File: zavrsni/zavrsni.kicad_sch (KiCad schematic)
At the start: 81 parts, among them J1 Barrel_Jack_MountingPin, J2 SameSky 6.35 horizontal jack, J3 USB_B, J4 SameSky 6.35 horizontal jack, SW1 EC11, U1 TL072, U10 TL072, U2 LM317_TO-220, U3 LM317_TO-220, U4 TL074, U6 WeAct STM32F411CEU6 v3.0, U7 TL074, U8 CS4271, U9 TL072

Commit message: KiCad 10
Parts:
- removed C1: 100n, Capacitor_THT:C_Disc_D5.0mm_W2.5mm_P5.00mm, symbol Device:C_Small
- removed R21: 10k, Resistor_THT:R_Axial_DIN0207_L6.3mm_D2.5mm_P2.54mm_Vertical, symbol Device:R
- removed U1, U10, U9: TL072, Package_DIP:DIP-8_W7.62mm, symbol Amplifier_Operational:TL072
- added C1: 47u, Capacitor_THT:CP_Radial_D5.0mm_P2.50mm, symbol Device:C_Polarized_Small
- added C26, C27: 10u, Capacitor_THT:CP_Radial_D5.0mm_P2.50mm, symbol Device:C_Polarized_Small
- added U1: TL074, Package_DIP:DIP-14_W7.62mm, symbol Amplifier_Operational:TL074
- added unit 5 of U4
- added unit 2 of U4
- added U9: LM358, Package_DIP:DIP-8_W7.62mm, symbol Amplifier_Operational:LM358
- C3: value 680u -> 10u; footprint Capacitor_THT:CP_Radial_D8.0mm_P2.50mm -> Capacitor_THT:CP_Radial_D5.0mm_P2.50mm
- R1, R2: value 51k -> 10k
- SW_BNK+1, SW_BNK-1, SW_PRE+1, SW_PRE-1, SW_VOL+1, SW_VOL-1: footprint Button_Switch_THT:SW_PUSH_6mm_H7.3mm -> Button_Switch_THT:SW_PUSH_6mm_H13mm
- U5: value ~ -> (none)
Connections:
- net GNDPWR: now also J1.3 (MountPin), C1.2, C26.2, C27.2; no longer J1.MP (MountPin)
- net GNDREF: now also C1.1, U9.1, U9.2 (-); no longer C3.1
- net IN: now also U1.5 (+)
- net VREF_ADC: now also U4.8, U4.9 (-)
- net at C8.1, R7.1, R8.1: now also U1.9 (-); no longer U4.2 (-)
- net at C8.2, R11.2, R8.2: now also U1.8; no longer U4.1
- net at R6.1: now also U1.6 (-), U1.7
- net at R4.2, R5.1, U2.1 (ADJ): now also C26.1
- net at C25.1: now also U7.1, U7.2 (-)
- net at C24.1, R28.2: now also U7.3 (+)
- net at C18.1, C20.1, U8.15 (VQ1): now also U4.10 (+)
- net at C6.1, R6.2: now also U1.10 (+); no longer U4.3 (+)
- net at R12.2, R13.1: now also U1.12 (+); no longer U4.10 (+)
- net at R24.2, R26.2: now also U4.12 (+)
- net at D1.2 (A), D2.1 (K), R11.1: now also U4.2 (-), U1.13 (-), U4.5 (+); no longer U4.13 (-), U4.9 (-), U7.3 (+)
- net at C23.1, R25.1, R27.2: now also U4.13 (-)
- net at R10.1, R9.2, U3.1 (ADJ): now also C27.1
- net at R1.1, R2.2: now also C3.1, U9.3 (+), U9.5 (+)
- net at R14.2, R15.1: now also U4.3 (+); no longer U4.12 (+)
- net at C23.2, R27.1, R28.1: now also U4.14
- net at D1.1 (K): now also U1.14; no longer U4.8
- net at D2.2 (A): now also U4.1; no longer U4.14
- new net: U9.6 (-), U9.7
- new net: C12.1, U4.6 (-), U4.7
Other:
- note added: "Napajanje"
- note removed: "Ulazni razdvojnik (buffer)"
- moved on the sheet: C10, C11, C12, C13, C14, C15, C16, C17, C18, C19, C2, C20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

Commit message: Started work on the PCB. Started drawing the codec/STM32 part of the layout.
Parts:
- removed U4, U7: TL074, Package_DIP:DIP-14_W7.62mm, symbol Amplifier_Operational:TL074
- added C28: 10u, Capacitor_THT:CP_Radial_D5.0mm_P2.50mm, symbol Device:C_Polarized_Small
- added C29, C30, C31, C33: 100n, Capacitor_THT:C_Disc_D5.0mm_W2.5mm_P5.00mm, symbol Device:C_Small
- added C32: 100u, Capacitor_THT:CP_Radial_D5.0mm_P2.50mm, symbol Device:C_Polarized_Small
- added D3, D4, D5, D6, D7, D8: LED, LED_THT:LED_D3.0mm, symbol Device:LED
- added JP_LIM1: SolderJumper_2_Open, Jumper:SolderJumper-2_P1.3mm_Open_RoundedPad1.0x1.5mm, symbol Jumper:SolderJumper_2_Open
- added R21: 100, Resistor_THT:R_Axial_DIN0207_L6.3mm_D2.5mm_P5.08mm_Vertical, symbol Device:R
- added R30, R31, R32, R33, R34, R35: 1k, Resistor_THT:R_Axial_DIN0207_L6.3mm_D2.5mm_P2.54mm_Vertical, symbol Device:R
- added TP_3V3, TP_5V1, TP_FILT1, TP_LIM1: Conn_01x01, Connector_PinHeader_2.54mm:PinHeader_1x01_P2.54mm_Vertical, symbol Connector_Generic:Conn_01x01
- added TP_CODEC1: Conn_01x05, Connector_PinHeader_2.54mm:PinHeader_1x05_P2.54mm_Vertical, symbol Connector_Generic:Conn_01x05
- added TP_OUT1: Conn_01x02, Connector_PinHeader_2.54mm:PinHeader_1x02_P2.54mm_Vertical, symbol Connector_Generic:Conn_01x02
- added unit 1 of U1
- added U10, U7: TL072, Package_DIP:DIP-8_W7.62mm, symbol Amplifier_Operational:TL072
- R16, R19: footprint Resistor_THT:R_Axial_DIN0207_L6.3mm_D2.5mm_P5.08mm_Vertical -> Resistor_THT:R_Axial_DIN0207_L6.3mm_D2.5mm_P10.16mm_Horizontal
- R17: footprint Resistor_THT:R_Axial_DIN0207_L6.3mm_D2.5mm_P5.08mm_Vertical -> Resistor_THT:R_Axial_DIN0207_L6.3mm_D2.5mm_P15.24mm_Horizontal
- R22: footprint Resistor_THT:R_Axial_DIN0207_L6.3mm_D2.5mm_P5.08mm_Vertical -> Resistor_THT:R_Axial_DIN0207_L6.3mm_D2.5mm_P2.54mm_Vertical
- R23: footprint Resistor_THT:R_Axial_DIN0207_L6.3mm_D2.5mm_P2.54mm_Vertical -> Resistor_THT:R_Axial_DIN0207_L6.3mm_D2.5mm_P5.08mm_Vertical
- U6: footprint Package_DIP:DIP-40_W15.24mm_Socket -> ljepi:STM32F411CEU6 WeAct V3.0
- renumbered J2 to JIN1, J4 to JOUT1
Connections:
- net +3V3: now also TP_3V3.1 (Pin_1)
- net +5V: now also TP_5V1.1 (Pin_1)
- net GNDPWR: now also J3.SH (Shield), U1.11 (V-), U9.4 (V-), C28.2, C29.2, C30.2, C31.2, C32.2, C33.2, D3.1 (K), D4.1 (K), D5.1 (K), D6.1 (K), D7.1 (K), D8.1 (K), U10.4 (V-), U7.4 (V-); no longer J3.5 (Shield)
- net IN: now also U1.3 (+); no longer U1.5 (+)
- net MCU.LRCK: now also TP_CODEC1.2 (Pin_2)
- net MCU.MCLK: now also TP_CODEC1.1 (Pin_1)
- net MCU.SCLK: now also TP_CODEC1.3 (Pin_3)
- net VCC: now also U1.4 (V+), U9.8 (V+), C29.1, C30.1, C31.1, C32.1, C33.1, R21.2, R30.1, R31.1, R32.1, R33.1, R34.1, R35.1, U10.8 (V+), U7.8 (V+); no longer R1.2, R12.1, R14.1
- net VREF_ADC: now also U7.6 (-), U7.7
- net at R22.1, U8.7 (SDIN): now also TP_CODEC1.5 (Pin_5)
- net at C8.1, R7.1, R8.1: now also U1.6 (-); no longer U1.9 (-)
- net at C8.2, R11.2, R8.2: now also U1.7; no longer U1.8
- net at D2.2 (A): now also U1.14
- net at D1.2 (A), D2.1 (K), R11.1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: now also U1.9 (-), JP_LIM1.1 (A), TP_LIM1.1 (Pin_1)
- net at R14.2, R15.1: now also U1.12 (+)
- net at C18.1, C20.1, U8.15 (VQ1): now also U7.5 (+)
- net at C14.1, C15.1, U8.22 (FILT+): now also TP_FILT1.1 (Pin_1)
- net at C21.1, U8.24 (AOUTA-): now also TP_OUT1.1 (Pin_1)
- net at C22.1, U8.25 (AOUTA+): now also TP_OUT1.2 (Pin_2)
- net at R20.1, U8.6 (SDOUT): now also TP_CODEC1.4 (Pin_4)
- net at C6.1, R6.2: now also U1.5 (+); no longer U1.10 (+)
- net at R12.2, R13.1: now also U1.10 (+); no longer U1.12 (+)
- net at C25.1: now also U10.6 (-), U10.7
- net at C24.1, R28.2: now also U10.5 (+)
- net at R24.2, R26.2: now also U10.3 (+)
- net at C12.1: now also U7.1, U7.2 (-)
- net at C23.1, R25.1, R27.2: now also U10.2 (-)
- net at C23.2, R27.1, R28.1: now also U10.1
- net at D1.1 (K): now also U1.8; no longer U1.14
- new net: D4.2 (A), R31.2
- new net: D6.2 (A), R33.2
- new net: D5.2 (A), R32.2
- new net: R6.1, U1.1, U1.2 (-)
- new net: D8.2 (A), R35.2
- new net: JP_LIM1.2 (B), U7.3 (+)
- new net: D7.2 (A), R34.2
- new net: D3.2 (A), R30.2
- new net VCCA: C28.1, R1.2, R12.1, R14.1, R21.1
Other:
- moved on the sheet: C1, C2, C3, C4, C6, C8, D1, D2, H1, H2, H3, H4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

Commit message: PCB almost done.
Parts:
- removed D3, D4, D5, D6, D7, D8: LED, LED_THT:LED_D3.0mm, symbol Device:LED
- removed R30, R31, R32, R33, R34, R35: 1k, Resistor_THT:R_Axial_DIN0207_L6.3mm_D2.5mm_P2.54mm_Vertical, symbol Device:R
- removed TP_3V3, TP_5V1: Conn_01x01, Connector_PinHeader_2.54mm:PinHeader_1x01_P2.54mm_Vertical, symbol Connector_Generic:Conn_01x01
- removed TP_CODEC1: Conn_01x05, Connector_PinHeader_2.54mm:PinHeader_1x05_P2.54mm_Vertical, symbol Connector_Generic:Conn_01x05
- added J2: Conn_01x05, Connector_PinHeader_2.54mm:PinHeader_1x05_P2.54mm_Vertical, symbol Connector_Generic:Conn_01x05
- added JP_3V3, JP_5V1: SolderJumper_2_Open, Jumper:SolderJumper-2_P1.3mm_Open_RoundedPad1.0x1.5mm, symbol Jumper:SolderJumper_2_Open
- R25: footprint Resistor_THT:R_Axial_DIN0207_L6.3mm_D2.5mm_P2.54mm_Vertical -> Resistor_THT:R_Axial_DIN0207_L6.3mm_D2.5mm_P10.16mm_Horizontal
- R26: footprint Resistor_THT:R_Axial_DIN0207_L6.3mm_D2.5mm_P2.54mm_Vertical -> Resistor_THT:R_Axial_DIN0207_L6.3mm_D2.5mm_P7.62mm_Horizontal
- R3: footprint Resistor_THT:R_Axial_DIN0207_L6.3mm_D2.5mm_P2.54mm_Vertical -> Resistor_THT:R_Axial_DIN0207_L6.3mm_D2.5mm_P5.08mm_Vertical
- R6: footprint Resistor_THT:R_Axial_DIN0207_L6.3mm_D2.5mm_P5.08mm_Vertical -> Resistor_THT:R_Axial_DIN0207_L6.3mm_D2.5mm_P7.62mm_Horizontal
- R8: footprint Resistor_THT:R_Axial_DIN0207_L6.3mm_D2.5mm_P5.08mm_Vertical -> Resistor_THT:R_Axial_DIN0207_L6.3mm_D2.5mm_P2.54mm_Vertical
- U2, U3: footprint Package_TO_SOT_THT:TO-220-3_Horizontal_TabDown -> Package_TO_SOT_THT:TO-220-3_Vertical
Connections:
- net +3V3: now also JP_3V3.2 (B); no longer R9.1, U3.2 (VO), U6.20 (3V3)
- net +5V: now also U3.2 (VO), JP_5V1.2 (B); no longer R4.1, U2.2 (VO), U3.3 (VI)
- net BTN.BNK+: now also U6.17 (B9); no longer U6.13 (B5)
- net BTN.BNK-: now also U6.16 (B8); no longer U6.12 (B4)
- net BTN.PRE+: now also U6.13 (B5); no longer U6.17 (B9)
- net BTN.PRE-: now also U6.12 (B4); no longer U6.16 (B8)
- net GNDPWR: now also SW1.S1; no longer SW1.S2
- net MCU.ADC_OUT: now also J2.3 (Pin_3)
- net MCU.DAC_IN: now also J2.2 (Pin_2)
- net MCU.RST: now also J2.1 (Pin_1)
- net MCU.DAC_IN0: now reaches R22.1, U8.7 (SDIN)
- net MCU.ADC_OUT0: now reaches R20.1, U8.6 (SDOUT)
- net MCU.SCLK0: now reaches R16.2, U6.2 (B13)
- net MCU.SCLK0: now also J2.4 (Pin_4)
- net at U6.24 (C15): now also SW1.S2; no longer SW1.S1
- net MCU.LRCK0: now reaches R17.2, U6.1 (B12)
- net MCU.LRCK0: now also J2.5 (Pin_5)
- new net: JP_3V3.1 (A), R9.1, U3.3 (VI)
- new net: JP_5V1.1 (A), R4.1, U2.2 (VO)
- no-connect marks 16 -> 32
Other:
- moved on the sheet: R10, R16, R17, R20, R4, R5, R9

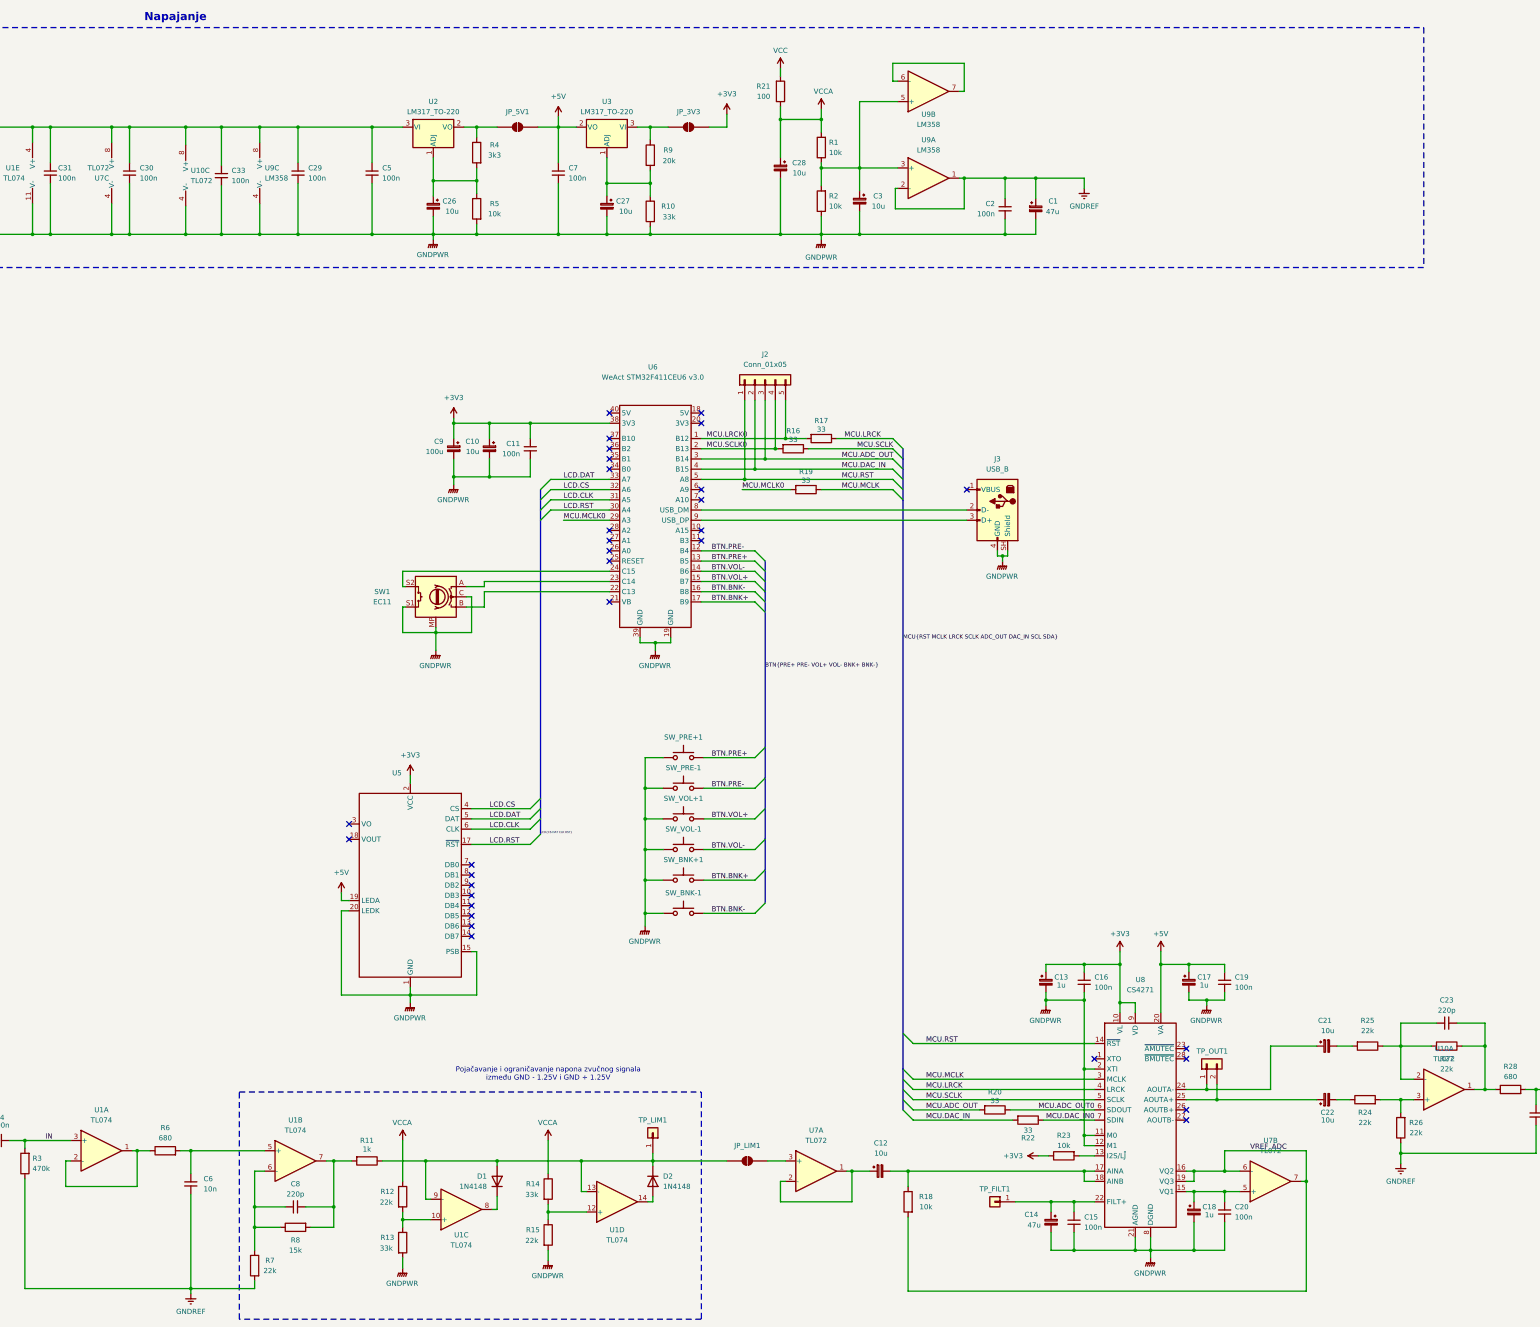
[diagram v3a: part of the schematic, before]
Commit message: PCB done. Code, PCB screw holes and 3D design left
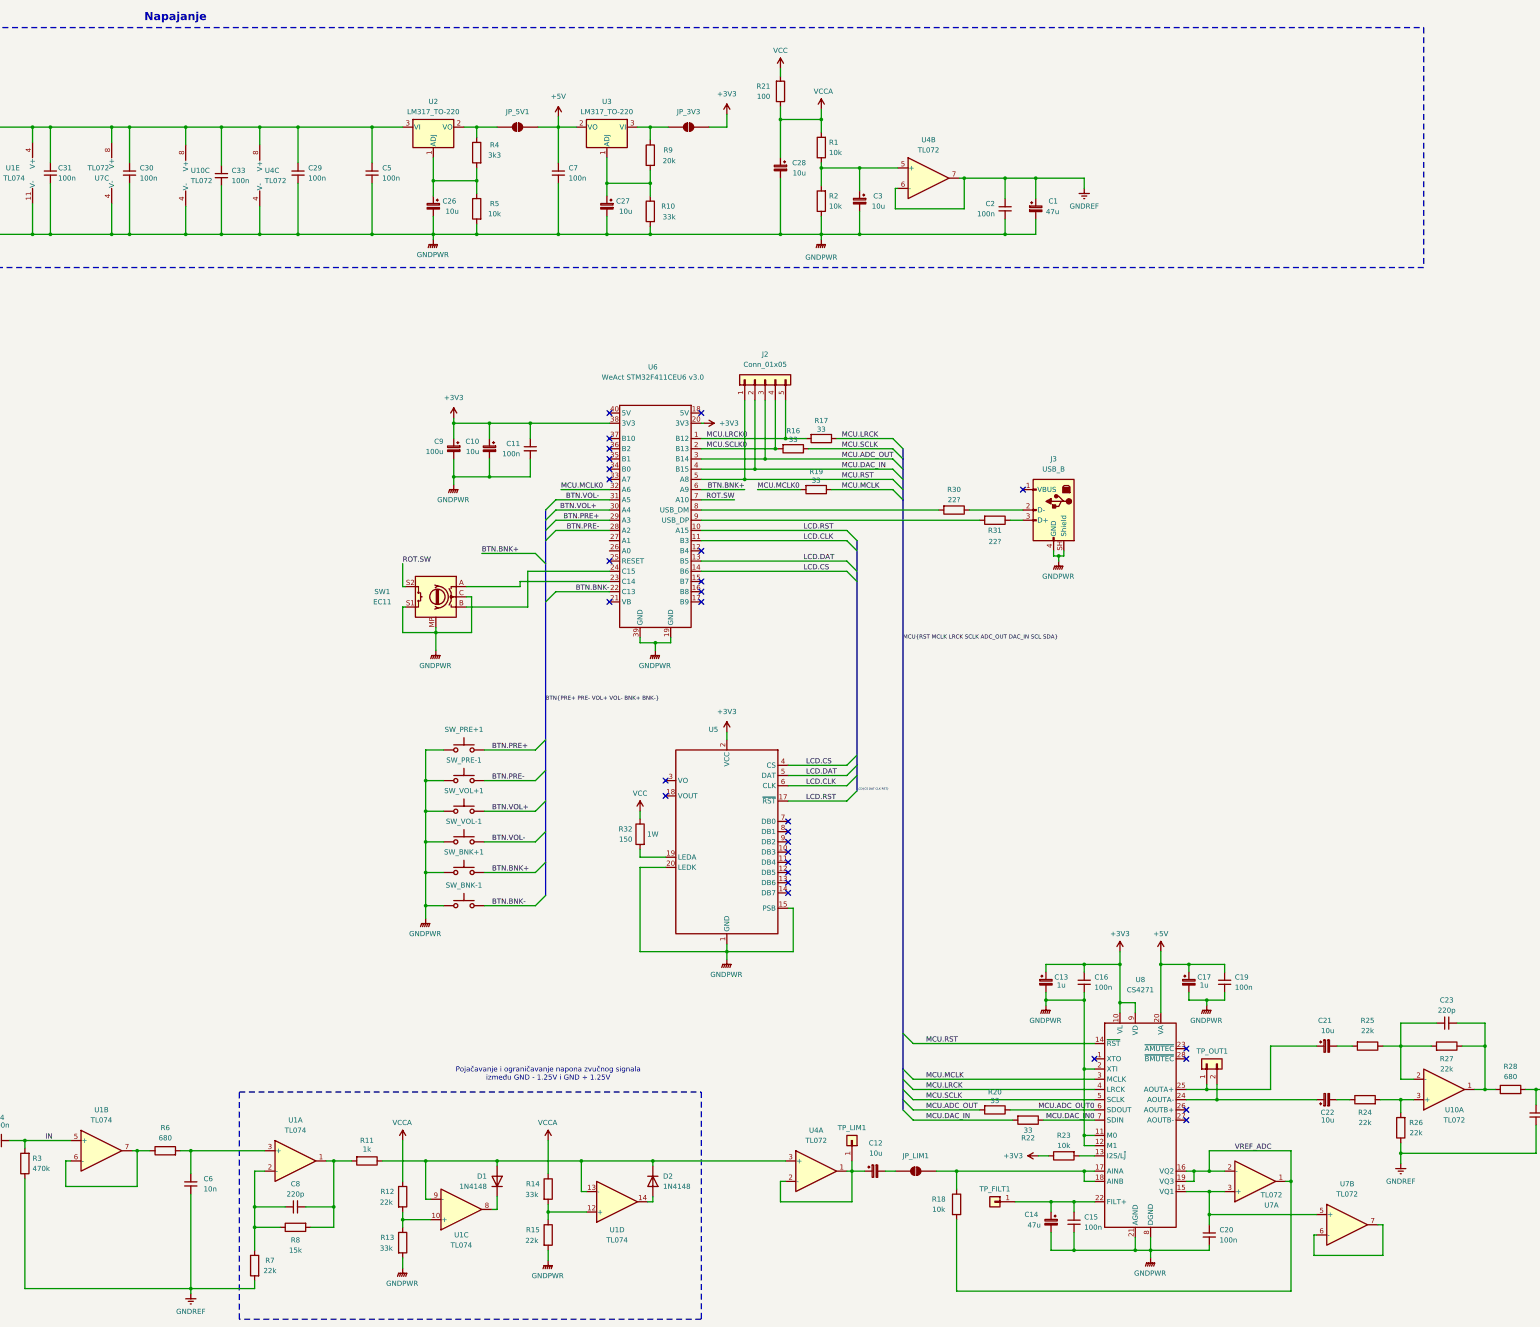
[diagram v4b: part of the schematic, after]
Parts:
- removed C18: 1u, Capacitor_THT:CP_Radial_D5.0mm_P2.50mm, symbol Device:C_Polarized_Small
- removed U9: LM358, Package_DIP:DIP-8_W7.62mm, symbol Amplifier_Operational:LM358
- added R30: 22?, Resistor_THT:R_Axial_DIN0207_L6.3mm_D2.5mm_P15.24mm_Horizontal, symbol Device:R
- added R31: 22?, Resistor_THT:R_Axial_DIN0207_L6.3mm_D2.5mm_P7.62mm_Horizontal, symbol Device:R
- added R32: 150, Resistor_THT:R_Axial_DIN0411_L9.9mm_D3.6mm_P12.70mm_Horizontal, symbol Device:R
- added U4: TL072, Package_DIP:DIP-8_W7.62mm, symbol Amplifier_Operational:TL072
- J3: footprint Connector_USB:USB_B_Lumberg_2411_02_Horizontal -> ljepi:USB B Female
- R1, R19: footprint Resistor_THT:R_Axial_DIN0207_L6.3mm_D2.5mm_P10.16mm_Horizontal -> Resistor_THT:R_Axial_DIN0207_L6.3mm_D2.5mm_P15.24mm_Horizontal
- R10: footprint Resistor_THT:R_Axial_DIN0207_L6.3mm_D2.5mm_P2.54mm_Vertical -> Resistor_THT:R_Axial_DIN0207_L6.3mm_D2.5mm_P5.08mm_Vertical
- R16, R2, R25: footprint Resistor_THT:R_Axial_DIN0207_L6.3mm_D2.5mm_P10.16mm_Horizontal -> Resistor_THT:R_Axial_DIN0207_L6.3mm_D2.5mm_P2.54mm_Vertical
- R17: footprint Resistor_THT:R_Axial_DIN0207_L6.3mm_D2.5mm_P15.24mm_Horizontal -> Resistor_THT:R_Axial_DIN0207_L6.3mm_D2.5mm_P2.54mm_Vertical
- R18: footprint Resistor_THT:R_Axial_DIN0207_L6.3mm_D2.5mm_P2.54mm_Vertical -> Resistor_THT:R_Axial_DIN0207_L6.3mm_D2.5mm_P10.16mm_Horizontal
- R20, R23, R28, R3: footprint Resistor_THT:R_Axial_DIN0207_L6.3mm_D2.5mm_P5.08mm_Vertical -> Resistor_THT:R_Axial_DIN0207_L6.3mm_D2.5mm_P2.54mm_Vertical
- R21: footprint Resistor_THT:R_Axial_DIN0207_L6.3mm_D2.5mm_P5.08mm_Vertical -> Resistor_THT:R_Axial_DIN0207_L6.3mm_D2.5mm_P7.62mm_Horizontal
- R26: footprint Resistor_THT:R_Axial_DIN0207_L6.3mm_D2.5mm_P7.62mm_Horizontal -> Resistor_THT:R_Axial_DIN0207_L6.3mm_D2.5mm_P5.08mm_Vertical
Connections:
- net +3V3: now also U6.20 (3V3)
- net +5V: no longer U5.19 (LEDA)
- net BTN.BNK+: now also U6.6 (A9); no longer U6.17 (B9)
- net BTN.BNK-: now also U6.22 (C13); no longer U6.16 (B8)
- net BTN.PRE+: now also U6.29 (A3); no longer U6.13 (B5)
- net BTN.PRE-: now also U6.28 (A2); no longer U6.12 (B4)
- net BTN.VOL+: now also U6.30 (A4); no longer U6.15 (B7)
- net BTN.VOL-: now also U6.31 (A5); no longer U6.14 (B6)
- net GNDPWR: now also U4.4 (V-)
- net GNDREF: now also U4.6 (-), U4.7
- net IN: now also U1.5 (+); no longer U1.3 (+)
- net LCD.CLK: now also U6.11 (B3); no longer U6.31 (A5)
- net LCD.CS: now also U6.14 (B6); no longer U6.32 (A6)
- net LCD.DAT: now also U6.13 (B5); no longer U6.33 (A7)
- net LCD.RST: now also U6.10 (A15); no longer U6.30 (A4)
- net MCU.MCLK0: now also U6.32 (A6); no longer U6.29 (A3)
- net VCC: now also R32.1, U4.8 (V+)
- net VREF_ADC: now also U7.1, U7.2 (-); no longer U7.6 (-), U7.7
- net at C8.1, R7.1, R8.1: now also U1.2 (-); no longer U1.6 (-)
- net at C8.2, R11.2, R8.2: now also U1.1; no longer U1.7
- net at C3.1, R1.1, R2.2: now also U4.5 (+)
- net at C20.1, U7.5 (+), U8.15 (VQ1): now also U7.3 (+)
- net at R18.1, U8.17 (AINA), U8.18 (AINB): now also JP_LIM1.2 (B); no longer C12.2
- net at C21.1, TP_OUT1.1 (Pin_1): now also U8.25 (AOUTA+); no longer U8.24 (AOUTA-)
- net at C22.1, TP_OUT1.2 (Pin_2): now also U8.24 (AOUTA-); no longer U8.25 (AOUTA+)
- net at C6.1, R6.2: now also U1.3 (+); no longer U1.5 (+)
- net at D1.2 (A), D2.1 (K), R11.1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: now also U4.3 (+); no longer JP_LIM1.1 (A), TP_LIM1.1 (Pin_1)
- net at SW1.B: now also U6.24 (C15); no longer U6.22 (C13)
- net ROT.SW: now reaches SW1.S2
- net ROT.SW: now also U6.7 (A10); no longer U6.24 (C15)
- net at J3.2 (D-): now also R30.1; no longer U6.8 (USB_DM)
- net at J3.3 (D+): now also R31.1; no longer U6.9 (USB_DP)
- new net: R6.1, U1.6 (-), U1.7
- new net: C12.2, JP_LIM1.1 (A)
- new net: C12.1, TP_LIM1.1 (Pin_1), U4.1, U4.2 (-)
- new net: R31.2, U6.9 (USB_DP)
- new net: R30.2, U6.8 (USB_DM)
- new net: R32.2, U5.19 (LEDA)
- new net: U7.6 (-), U7.7
- no-connect marks 32 -> 29
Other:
- moved on the sheet: C12, C20, J3, R18, R19, U5

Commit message: PCB work.
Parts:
- added C18: 68n, Capacitor_THT:C_Disc_D5.0mm_W2.5mm_P2.50mm, symbol Device:C_Small
- added H5, H6, H7: MountingHole_Pad, MountingHole:MountingHole_2.1mm, symbol Mechanical:MountingHole_Pad
- added R33: 100, Resistor_THT:R_Axial_DIN0207_L6.3mm_D2.5mm_P2.54mm_Vertical, symbol Device:R
- C29: footprint Capacitor_THT:C_Disc_D5.0mm_W2.5mm_P5.00mm -> Capacitor_THT:C_Disc_D5.0mm_W2.5mm_P2.50mm
- H1, H2, H3, H4: footprint MountingHole:MountingHole_3.2mm_M3_Pad -> MountingHole:MountingHole_2.1mm
- R18: value 10k -> 100k
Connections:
- net GNDPWR: now also C18.2, H5.1, H6.1, H7.1
- net at JP_LIM1.2 (B), U8.17 (AINA), U8.18 (AINB): no longer R18.1
- net at C12.2, JP_LIM1.1 (A): now also R18.1, TP_LIM1.1 (Pin_1)
- net at U4.1, U4.2 (-): now also R33.1; no longer C12.1, TP_LIM1.1 (Pin_1)
- net at D1.2 (A), D2.1 (K), R11.1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: no longer U1.13 (-), U1.9 (-)
- net at D2.2 (A), U1.14: now also U1.13 (-)
- net at D1.1 (K), U1.8: now also U1.9 (-)
- new net: C12.1, C18.1, R33.2
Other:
- moved on the sheet: C12, JP_LIM1, R12, R13, R14, R15, R18, TP_LIM1, U1C, U1D, U4A
